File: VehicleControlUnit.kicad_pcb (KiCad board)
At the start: 2 copper layers, 86.6 x 100 mm, 101 parts, among them Con1 LED, Con2 LED, J1 Conn_01x02, J10 Conn_01x04, J11 Conn_01x04, J12 SFH11-PBPC-D05-ST-BK, J13 SFH11-PBPC-D05-ST-BK, J2 Conn_01x02, J3 Conn_01x02, J5 SFH11-PBPC-D05-ST-BK, J6 Conn_01x04, J7 Conn_01x04, J8 Conn_01x04, J9 USB_C_Receptacle_USB2.0_16P, Q1 PSMN8R5-40MSDX, Q2 IRLML0030, Q3 IRLML0030, SW1 RESET, SW2 BOOT, U1 LM74501-Q1, U2 TLV1117LV33DCYR, U4 ESP32-C6-MINI-1/U, U5 TCMT1106, U6 TCMT1106

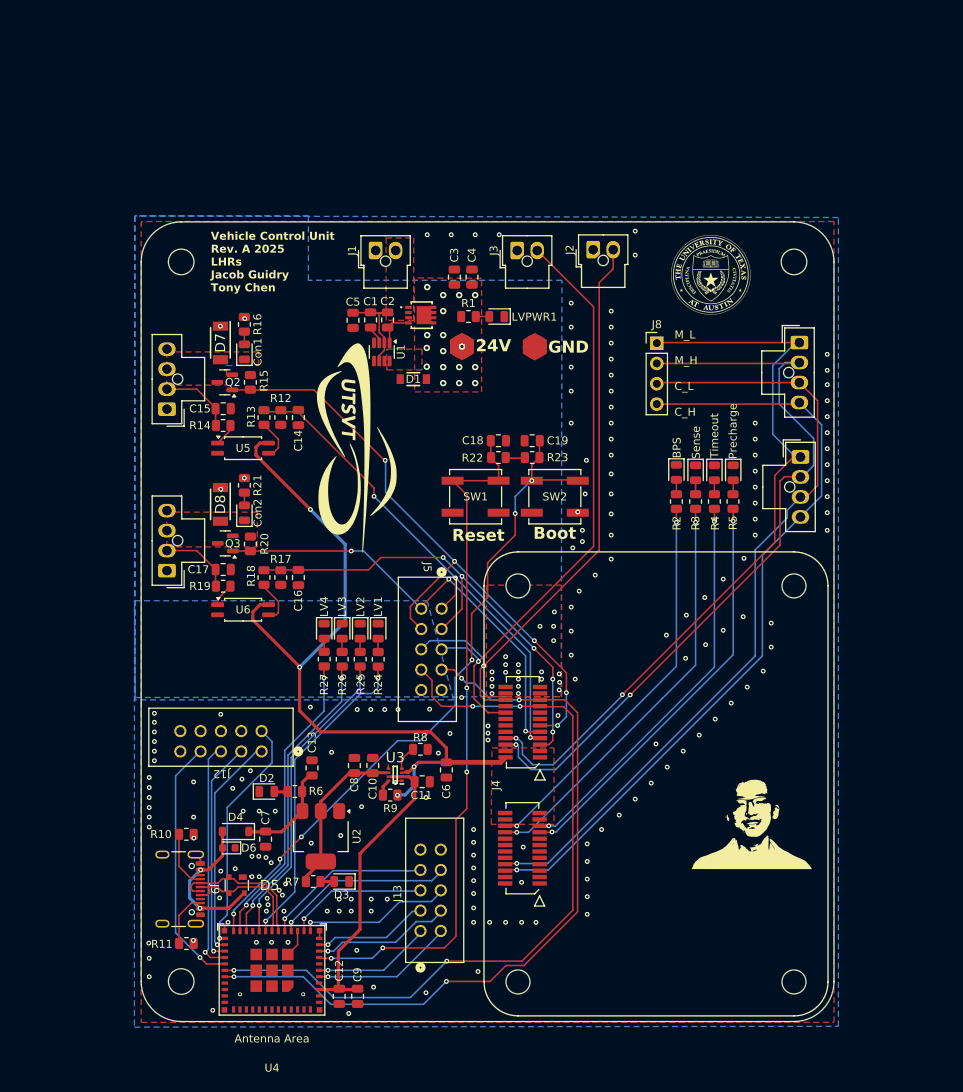
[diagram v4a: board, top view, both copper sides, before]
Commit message: shrunk the board by 7mm
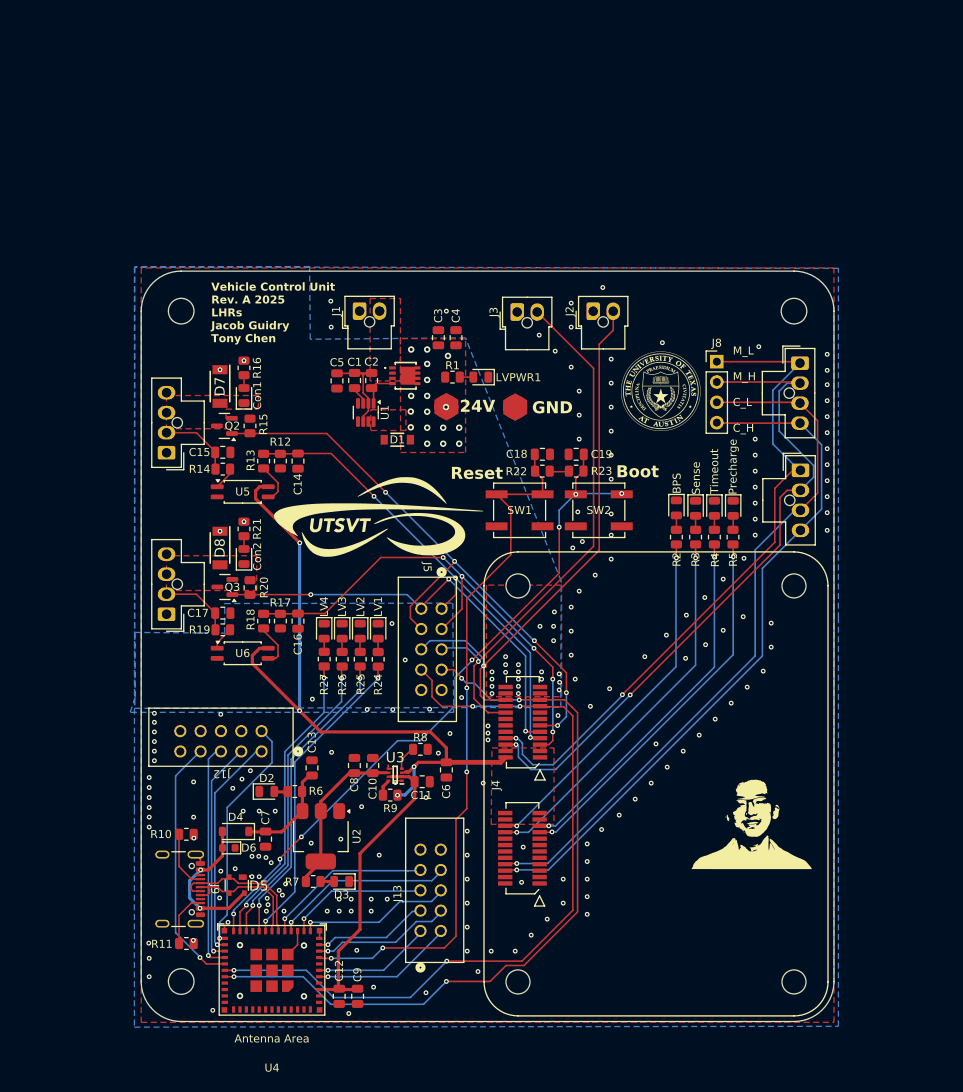
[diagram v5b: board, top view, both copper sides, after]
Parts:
- added G***: LOGO, UTSVT_Logos:Hallock_Image_Tiny, B.Cu at (169.7, 91.3)
- moved G*** 15.8 mm to (174.2, 63.0)
- moved G*** 9.02 mm to (139.1, 78.8), turned to 0 degrees
- moved G*** 8.54 mm to (143.0, 63.0)
- moved LVGND_TP1 7.94 mm to (156.0, 65.0)
- moved J8 7.85 mm to (181.2, 59.3)
- moved C3 7.83 mm to (146.4, 56.3)
- moved C4 7.83 mm to (148.6, 56.3)
- moved C5 7.83 mm to (133.7, 61.7)
- moved D1 7.83 mm to (141.3, 69.1)
- moved J1 7.83 mm to (136.6, 53.0)
- moved LVPWR1 7.83 mm to (151.7, 61.2)
- moved Q1 7.83 mm to (142.3, 61.1)
- moved R1 7.83 mm to (148.2, 61.2)
- moved C1 7.83 mm to (135.9, 61.7)
- moved C2 7.83 mm to (138.1, 61.7)
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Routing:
- net /C_CAN_H: track 97.9 -> 87.1 mm
- net /M_CAN_H: track 96.5 -> 85.8 mm
- net 3V3_LSOM: track 95.4 -> 85.3 mm
- net /M_CAN_L: track 95.5 -> 86.4 mm
- net /C_CAN_L: track 98.8 -> 90.3 mm
- net /Motor_Voltage: track 75.4 -> 67.7 mm
- net /Batt_Voltage: track 76.0 -> 68.4 mm
- net /M_Enable: track 79.2 -> 74.7 mm
- net /LED4: track 51.6 -> 47.1 mm
- net /LED2: track 51.9 -> 47.5 mm
- net /LED1: track 49.4 -> 44.9 mm
- net /LED3: track 49.8 -> 45.3 mm
- net /MPre_Sense: track 60.7 -> 63.4 mm
- net /M_Sense: track 62.8 -> 60.1 mm
- net /MPre_Enable: track 56.8 -> 54.6 mm
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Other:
- board size 86.6 x 100 mm -> 86.6 x 93.8 mm

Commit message: cubemx stuff
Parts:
- removed the G*** at (169.7, 91.3)
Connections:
- J4 pad 16: /Motor_Voltage -> /MPre_Enable
- J4 pad 17: /ESP_RX -> /ESP_TX
- J4 pad 19: /ESP_TX -> /ESP_RX
- J4 pad 9: /MPre_Enable -> /Motor_Voltage
- J5 pad 7: /ESP_TX -> /ESP_RX
- J5 pad 8: /ESP_RX -> /ESP_TX
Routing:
- net /Motor_Voltage: track 67.7 -> 73.0 mm, vias 1 -> 3
- net /ESP_TX: track 94.7 -> 97.3 mm
- net /ESP_RX: track 97.0 -> 95.0 mm
- net /MPre_Enable: track 54.6 -> 52.8 mm
